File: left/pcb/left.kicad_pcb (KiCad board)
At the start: 2 copper layers, 100 x 75 mm, 23 parts, among them J1 Jack, U1 Hall_Sensor, U10 Hall_Sensor, U11 Hall_Sensor, U2 Hall_Sensor, U3 Hall_Sensor, U4 Hall_Sensor, U5 Hall_Sensor, U6 Hall_Sensor, U7 74HC4051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

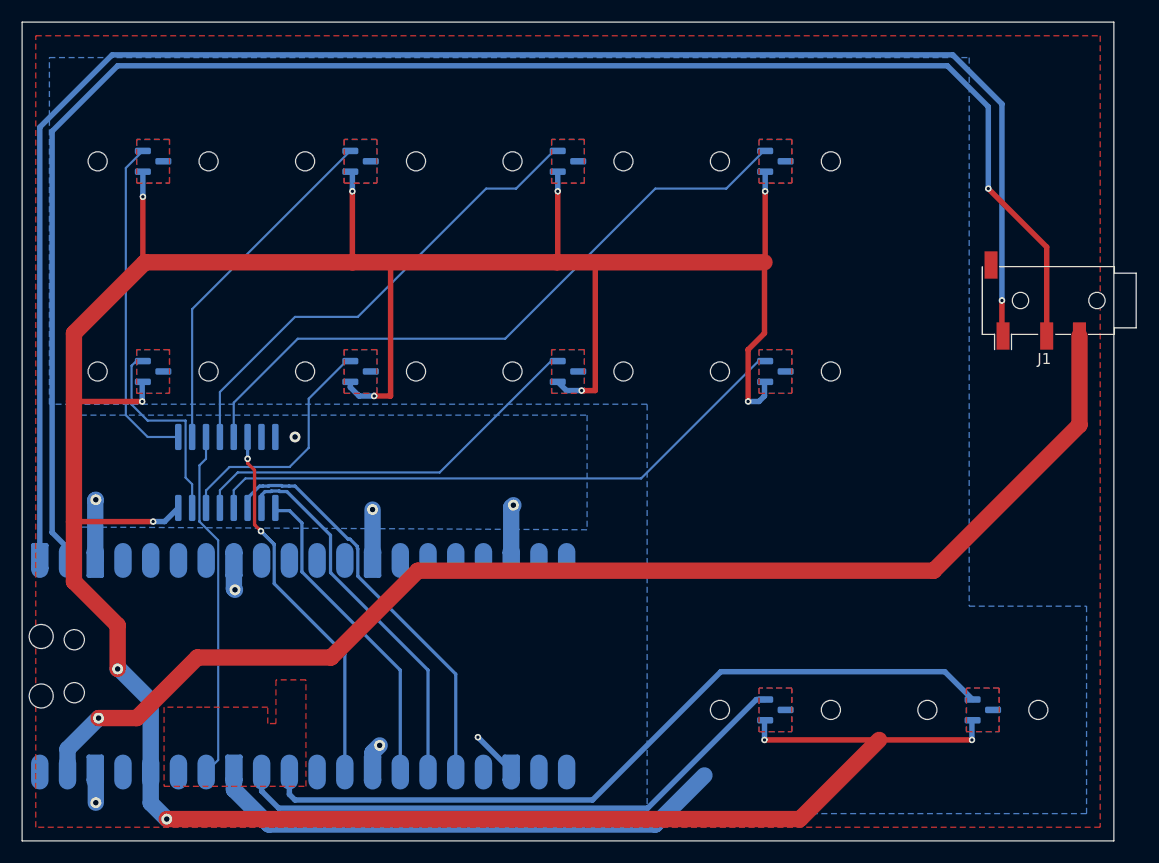
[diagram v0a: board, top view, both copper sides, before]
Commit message: move jack to the other side of the pcb
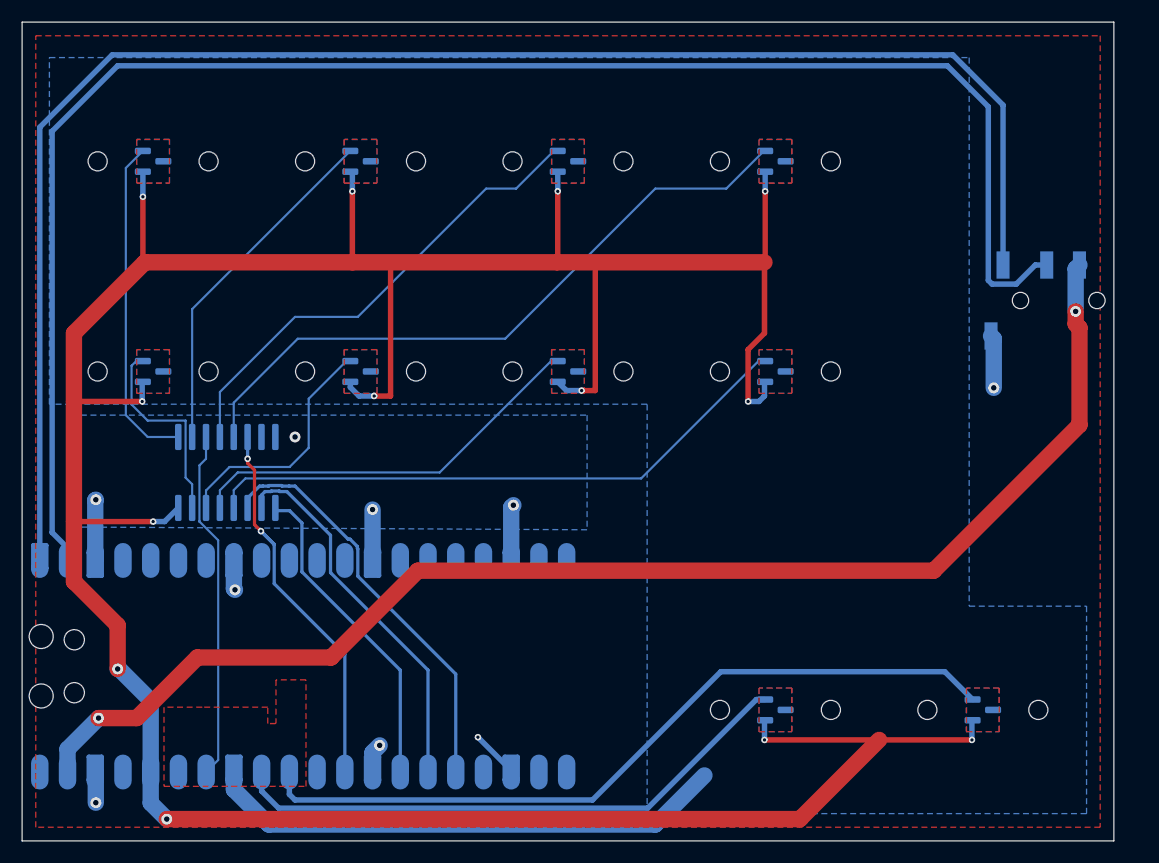
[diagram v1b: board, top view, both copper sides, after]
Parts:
- J1: moved to B.Cu
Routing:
- net /VSYS: track 115.2 -> 122.0 mm, vias 1 -> 2
- net /UART-TX: track 153.7 -> 147.2 mm, vias 1 -> 0
- net GND: track 28.1 -> 33.0 mm, vias 8 -> 9
- net /UART-RX: track 153.7 -> 152.7 mm, vias 1 -> 0
